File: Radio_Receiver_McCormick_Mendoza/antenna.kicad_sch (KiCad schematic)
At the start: 0 parts

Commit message: Merge conflict resolution.
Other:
- title: (none) -> Radio Receiver
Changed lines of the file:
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@@
 	(paper "A4")
 	(title_block
+		(title "Radio Receiver")
 		(date "2026-04-19")
 		(rev "0.0.1")

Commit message: Propogated Title Block Fields
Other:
- company: (none) -> Walla Walla University
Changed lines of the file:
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@@
 		(date "2026-04-19")
 		(rev "0.0.1")
+		(company "Walla Walla University")
 		(comment 2 "Daniel Mendoza")
 		(comment 3 "Jeffrey McCormick")

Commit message: Added basic antenna and bandpass filter schematic.
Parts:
- added C2, C3, C4: C, Capacitor_SMD:C_0805_2012Metric, symbol SDRReciever-rescue:C-Device-SDRReciever-rescue
- added C5: 0.1u, Capacitor_SMD:C_0805_2012Metric, symbol SDRReciever-rescue:C-Device-SDRReciever-rescue
- added J5: Conn_Coaxial, Connector_Coaxial:BNC_Amphenol_B6252HB-NPP3G-50_Horizontal, symbol SDRReciever-rescue:Conn_Coaxial-Connector-SDRReciever-rescue
- added J5: FIL_IN, Connector_PinHeader_2.54mm:PinHeader_1x01_P2.54mm_Vertical, symbol SDRReciever-rescue:Conn_01x01-Connector_Generic-SDRReciever-rescue
- added J8: FIL_OUT, Connector_PinHeader_2.54mm:PinHeader_1x01_P2.54mm_Vertical, symbol SDRReciever-rescue:Conn_01x01-Connector_Generic-SDRReciever-rescue
- added JP1: Jumper_NC_Small, Connector_PinHeader_2.54mm:PinHeader_1x02_P2.54mm_Vertical, symbol SDRReciever-rescue:Jumper_NC_Small-Device-SDRReciever-rescue
- added L1, L3: L, Inductor_THT:L_Toroid_Vertical_L13.0mm_W6.5mm_P5.60mm, symbol SDRReciever-rescue:L-Device-SDRReciever-rescue
- added L2: L, Inductor_THT:L_Toroid_Vertical_L10.0mm_W5.0mm_P5.08mm, symbol SDRReciever-rescue:L-Device-SDRReciever-rescue
- added R6, R7: 10k, Resistor_SMD:R_0805_2012Metric, symbol SDRReciever-rescue:R-Device-SDRReciever-rescue
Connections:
- new net: C4.2, L3.1
- new net: C3.2, C4.1, L1.2, L2.1
- new net: C2.2, L1.1
- new net: J5.2 (Ext), JP1.2
- new net: C2.1, J5.1 (In), J5.1 (Pin_1)
- new net BPF_OUT: J8.1 (Pin_1), L3.2, R6.1, R7.2
- new net GND: C3.1, C5.2, JP1.1, L2.2, R7.1
- new net VDDA: C5.1, R6.2
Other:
- note added: "Antenna Connector"
- note added: "Jumper for preventing ground loops"
- note added: "T37-6 Toroid: [NUM] turns"
- note added: "T50-6 Toroid: [NUMBER] turns"
- note added: "T50-6 Toroid: [NUM] turns"
- note added: "Test point pad"
- note added: "Toroid Info: T37-6: 3nH per turns^2 T50-6: 4nH per turns^2 See datasheet for more info"
- note added: "[FREQ RANGE] ([FILTER ORDER] Order, Series-First [FILTER NAME]) By doing Series-First, DC signals cannot pass through the capacitor (C2), allowing better control over the DC offset going into the op-amps"

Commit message: Added Bibliography entry
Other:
- note added: "0.5 MHz - 10 MHz (3rd Order, Series-First Bessel filter) By doing Series-First, DC signals cannot pass through the capacitor (C2), allowing better control over the DC offset going into the op-amps"
- note removed: "[FREQ RANGE] ([FILTER ORDER] Order, Series-First [FILTER NAME]) By doing Series-First, DC signals cannot pass through the capacitor (C2), allowing better control over the DC offset going into the op-amps"
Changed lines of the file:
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@@
 		)
 	)
-	(text "[FREQ RANGE] ([FILTER ORDER] Order, Series-First [FILTER NAME])\nBy doing Series-First, DC signals cannot pass through the capacitor (C2), \nallowing better control over the DC offset going into the op-amps"
+	(text "0.5 MHz - 10 MHz (3rd Order, Series-First Bessel filter)\nBy doing Series-First, DC signals cannot pass through the capacitor (C2), \nallowing better control over the DC offset going into the op-amps"
 		(exclude_from_sim no)
 		(at 101.6 71.755 0)

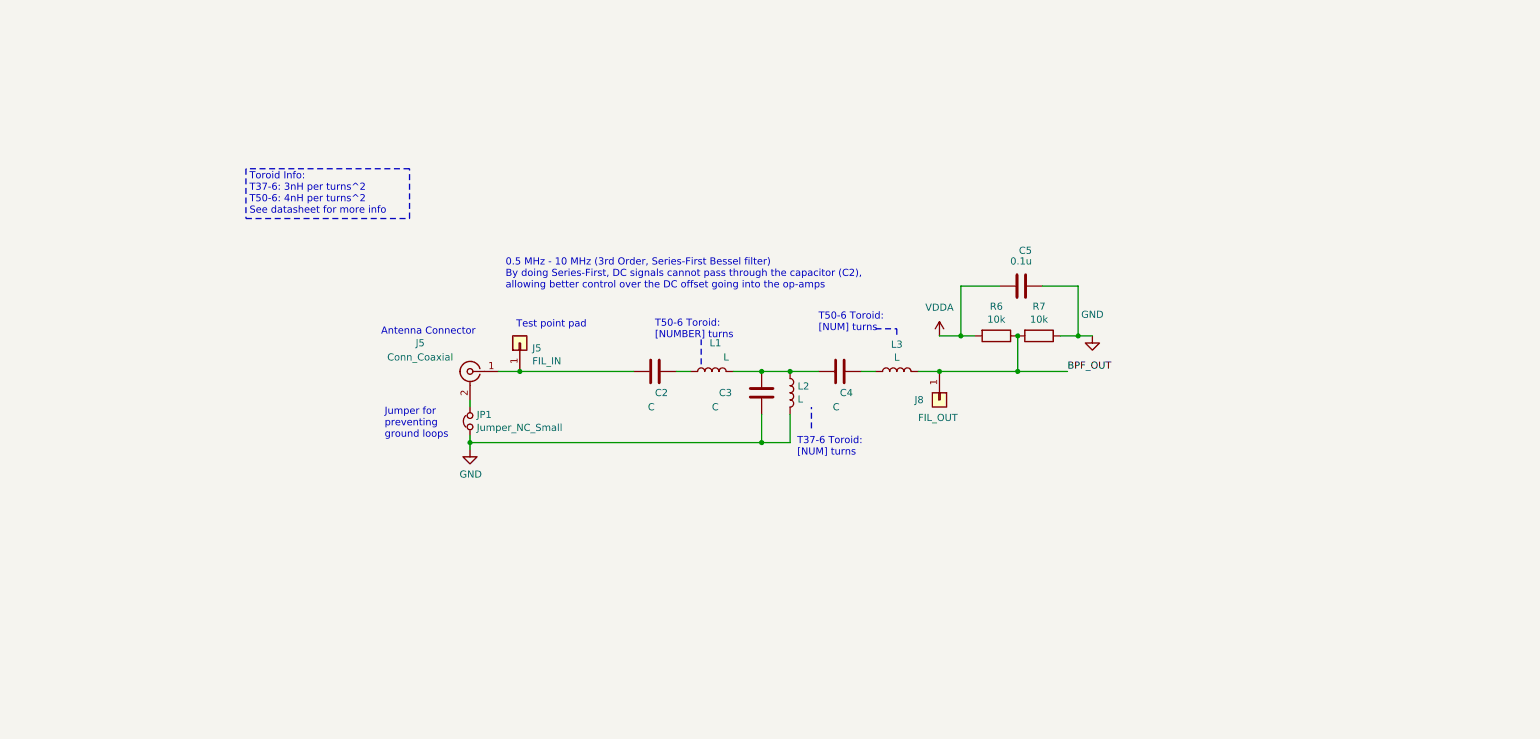
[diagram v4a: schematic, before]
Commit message: Added switchable antenna filters and photos.
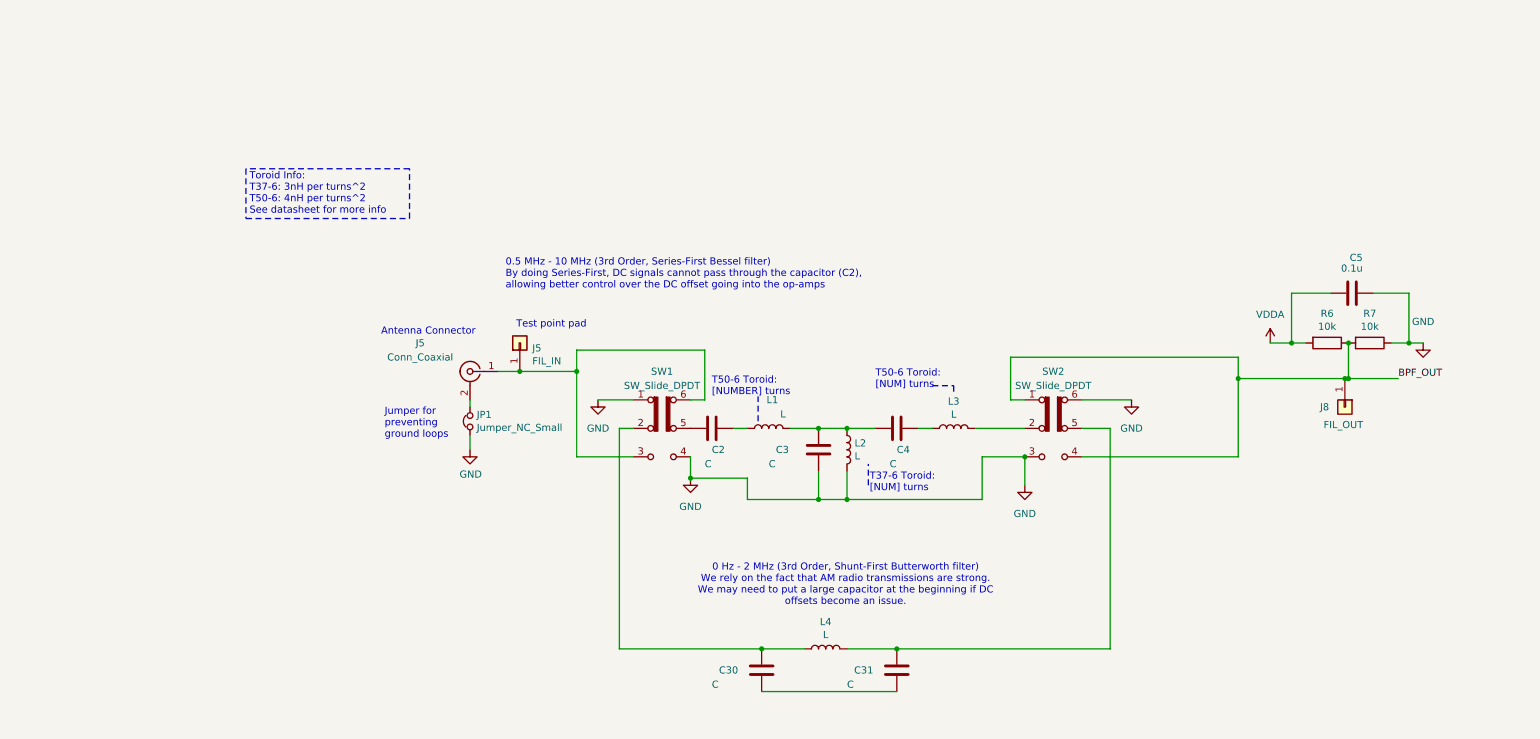
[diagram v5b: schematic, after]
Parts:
- added C30, C31: C, Capacitor_SMD:C_0805_2012Metric, symbol SDRReciever-rescue:C-Device-SDRReciever-rescue
- added L4: L, Inductor_THT:L_Toroid_Vertical_L13.0mm_W6.5mm_P5.60mm, symbol SDRReciever-rescue:L-Device-SDRReciever-rescue
- added SW1, SW2: SW_Slide_DPDT, symbol Switch:SW_Slide_DPDT
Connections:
- net BPF_OUT: now also SW2.1 (A), SW2.4 (A); no longer L3.2
- net GND: now also SW1.1 (A), SW1.4 (A), SW2.3 (C), SW2.6 (C)
- net at J5.1 (In), J5.1 (Pin_1): now also SW1.3 (C), SW1.6 (C); no longer C2.1
- new net: L3.2, SW2.2 (B)
- new net: C31.2, L4.2, SW2.5 (B)
- new net: C30.2, L4.1, SW1.2 (B)
- new net: C2.1, SW1.5 (B)
- new net: C30.1, C31.1
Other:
- note added: "0 Hz - 2 MHz (3rd Order, Shunt-First Butterworth filter) We rely on the fact that AM radio transmissions are strong. We may need to put a large capacitor at the beginning if DC offsets become an issue."
- moved on the sheet: C2, C3, C4, C5, J8, L1, L2, L3, R6, R7

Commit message: Schematic connection edits
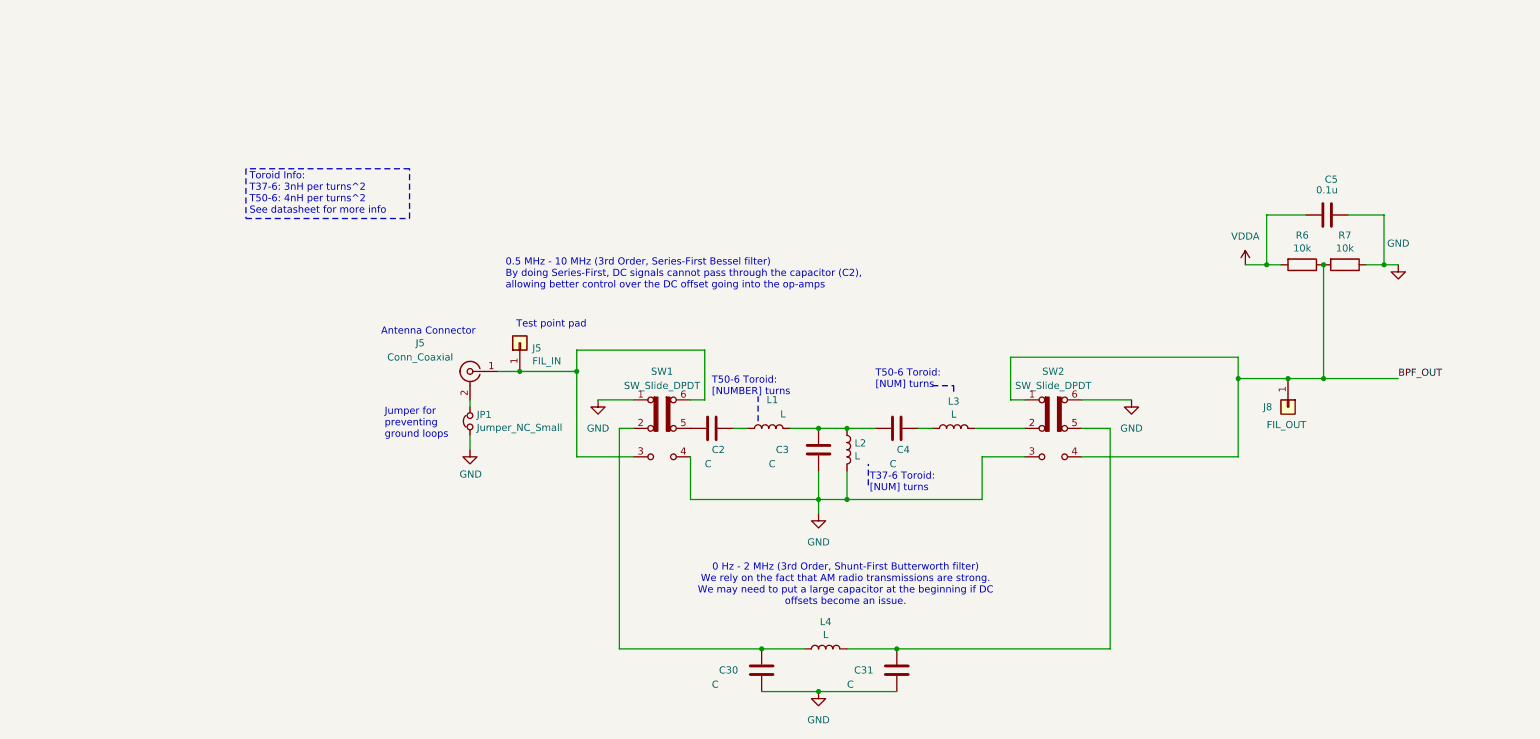
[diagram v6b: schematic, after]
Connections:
- net GND: now also C30.1, C31.1
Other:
- moved on the sheet: C5, J8, R6, R7

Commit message: Schematic edits power and signal systems
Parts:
- added C35, C36: 100nF, PCM_JLCPCB:C_0805, symbol PCM_JLCPCB-Capacitors:0805,100nF
- added C37: C, Capacitor_SMD:C_0805_2012Metric, symbol SDRReciever-rescue:C-Device-SDRReciever-rescue
- added T1: Transformer_1P_SS, symbol Device:Transformer_1P_SS
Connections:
- net GND: now also C35.1; no longer C3.1, C30.1, C31.1, JP1.1, L2.2, SW1.1 (A), SW1.4 (A), SW2.3 (C), SW2.6 (C)
- net VDDA: now also C36.1
- net at C30.2, L4.1: now also C37.2; no longer SW1.2 (B)
- net BPF_OUT: no longer names the net of J8.1 (Pin_1), SW2.1 (A), SW2.4 (A)
- net BPF_OUT: now also T1.1 (AA); no longer R6.1, R7.2
- new net: C35.2, C36.2, R6.1, R7.2, T1.4 (SC)
- new net: C37.1, SW1.2 (B)
- new net BPF_OUT1: T1.5 (SB)
- new net BPF_OUT2: T1.3 (SA)
- new net GNDA: C3.1, C30.1, C31.1, JP1.1, L2.2, SW1.1 (A), SW1.4 (A), SW2.3 (C), SW2.6 (C), T1.2 (AB)
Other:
- note added: "Blocking Capacitor to stop the DC from getting to the antenna."
- note added: "GNDA is the Antenna Ground It must be separate from the device ground (GND) to prevent ground loops."
- note added: "T50-6 Toroid: [NUM_1]/[NUM_2] turns"
- moved on the sheet: C2, C3, C30, C31, C4, C5, J5, J8, JP1, L1, L2, L3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

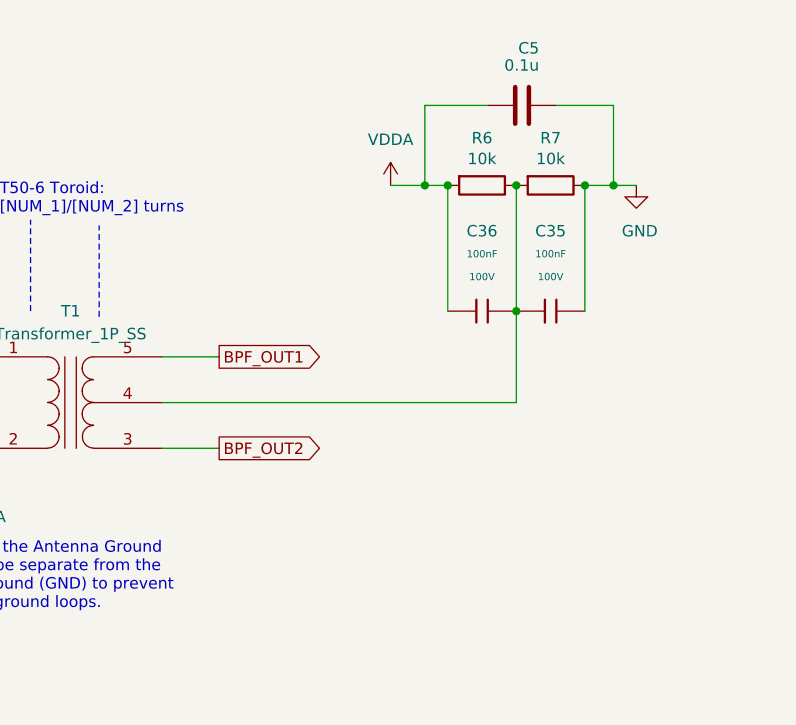
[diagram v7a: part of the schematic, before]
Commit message: Added reference voltage stability by buffer amp
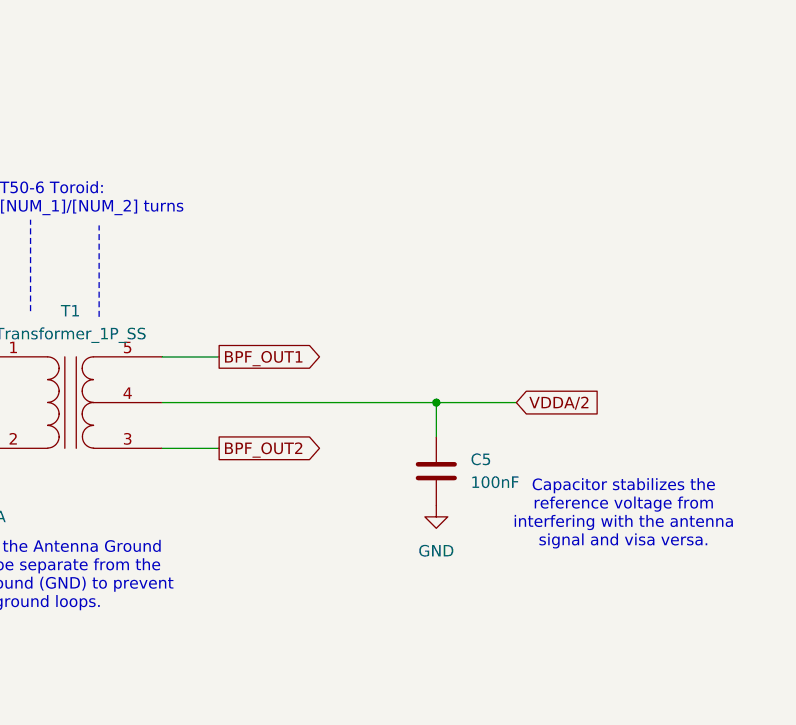
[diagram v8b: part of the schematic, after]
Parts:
- removed C35, C36: 100nF, PCM_JLCPCB:C_0805, symbol PCM_JLCPCB-Capacitors:0805,100nF
- removed C5: 0.1u, Capacitor_SMD:C_0805_2012Metric, symbol SDRReciever-rescue:C-Device-SDRReciever-rescue
- removed R6, R7: 10k, Resistor_SMD:R_0805_2012Metric, symbol SDRReciever-rescue:R-Device-SDRReciever-rescue
- added C5: 100nF, PCM_JLCPCB:C_1206, symbol Device:C
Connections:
- net GND: now also C5.2
- net VDDA/2: now reaches T1.4 (SC)
- net VDDA/2: now also C5.1
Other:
- note added: "Capacitor stabilizes the reference voltage from interfering with the antenna signal and visa versa."
